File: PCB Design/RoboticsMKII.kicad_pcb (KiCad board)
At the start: 4 copper layers, 93 parts, among them CON1 USB, CON2 BARREL_JACK, P1 Power Sel, P10 CONN_02X12, P11 DAC, P12 Reed, P13 SPI, P14 ICSP, P15 Gnd, P16 UART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

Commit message: Some changes?
Signed-off-by: Kolijn Wolfaardt <kolijn.wolfaardt@gmail.com>
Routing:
- net (no net): track 5.21 -> 0.13 mm, vias 15 -> 16
- net /mcu/MOT2_D1: track 39.0 -> 40.8 mm
- net GND: track 589.0 -> 588.5 mm
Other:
- board text added: "v1.00"
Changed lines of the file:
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@@
     (area 108.284333 35.228 170.003334 143.996)
     (thickness 1.6)
-    (drawings 6)
-    (tracks 1643)
+    (drawings 7)
+    (tracks 1646)
     (zones 0)
     (modules 93)
@@
     (mod_text_size 0.7 0.7)
     (mod_text_width 0.1)
-    (pad_size 4 4)
-    (pad_drill 3)
+    (pad_size 3.50012 3.50012)
+    (pad_drill 2.99974)
     (pad_to_mask_clearance 0)
     (aux_axis_origin 0 0)
@@
     (visible_elements FFFFF7FF)
     (pcbplotparams
-      (layerselection 0x000f0_80000007)
-      (usegerberextensions false)
+      (layerselection 0x001f0_80000007)
+      (usegerberextensions true)
       (excludeedgelayer true)
       (linewidth 0.100000)
-      (plotframeref true)
+      (plotframeref false)
       (viasonmask false)
       (mode 1)
@@
     (fp_line (start 7.00024 4.50088) (end 7.00024 -4.50088) (layer F.SilkS) (width 0.15))
     (fp_line (start 7.00024 -4.50088) (end -7.50062 -4.50088) (layer F.SilkS) (width 0.15))
-    (pad 1 thru_hole rect (at 6.20014 0 270) (size 3.50012 3.50012) (drill oval 1.00076 2.99974) (layers *.Cu *.Mask F.SilkS)
+    (pad 1 thru_hole rect (at 6.20014 0 270) (size 3.50012 3.50012) (drill oval 2.99974) (layers *.Cu *.Mask F.SilkS)
       (net 21 "Net-(CON2-Pad1)"))
-    (pad 2 thru_hole rect (at 0.20066 0 270) (size 3.50012 3.50012) (drill oval 1.00076 2.99974) (layers *.Cu *.Mask F.SilkS)
+    (pad 2 thru_hole rect (at 0.20066 0 270) (size 3.50012 3.50012) (drill oval 2.99974) (layers *.Cu *.Mask F.SilkS)
       (net 2 GND))
-    (pad 3 thru_hole rect (at 3.2004 4.699 270) (size 3.50012 3.50012) (drill oval 2.99974 1.00076) (layers *.Cu *.Mask F.SilkS)
+    (pad 3 thru_hole rect (at 3.2004 4.699 270) (size 3.50012 3.50012) (drill oval 2.99974) (layers *.Cu *.Mask F.SilkS)
       (net 22 "Net-(CON2-Pad3)"))
   )
@@
     )
   )
+  (gr_text v1.00 (at 145.796 90.932) (layer F.SilkS)
+    (effects (font (size 0.7 0.7) (thickness 0.12)))
+  )
   (gr_text https://github.com/KolijnWolfaardt/RoBoC (at 138.43 117.856) (layer F.SilkS)
     (effects (font (size 0.7 0.7) (thickness 0.12)))
@@
   (via (at 115.316 97.536) (size 0.6) (layers F.Cu B.Cu) (net 0))
   (via (at 152.908 64.516) (size 0.6) (layers F.Cu B.Cu) (net 0))
-  (via (at 116.84 82.55) (size 0.6) (layers F.Cu B.Cu) (net 0))
-  (segment (start 121.92 82.55) (end 116.84 82.55) (width 0.25) (layer In2.Cu) (net 0))
   (via (at 117.348 50.419) (size 0.6) (layers F.Cu B.Cu) (net 0))
   (via (at 119.888 48.133) (size 0.6) (layers F.Cu B.Cu) (net 0))
@@
   (via (at 139.573 52.832) (size 0.6) (layers F.Cu B.Cu) (net 0))
   (via (at 151.384 61.722) (size 0.6) (layers F.Cu B.Cu) (net 0))
+  (via (at 116.586 82.55) (size 0.6) (layers F.Cu B.Cu) (net 0))
+  (via (at 126.746 82.423) (size 0.6) (layers F.Cu B.Cu) (net 0))
   (via (at 141.478 49.53) (size 0.6) (layers F.Cu B.Cu) (net 1))
   (segment (start 143.48 48.29) (end 142.24 49.53) (width 0.4) (layer B.Cu) (net 1))
@@
   (segment (start 153.825 51.661) (end 154.051 51.435) (width 0.25) (layer B.Cu) (net 2))
   (segment (start 146.304 96.901) (end 143.129 96.901) (width 0.25) (layer B.Cu) (net 2))
-  (segment (start 129.45 65.095) (end 132.263 65.095) (width 0.25) (layer F.Cu) (net 2))
-  (segment (start 132.842 64.516) (end 132.842 62.23) (width 0.25) (layer F.Cu) (net 2))
-  (segment (start 132.263 65.095) (end 132.842 64.516) (width 0.25) (layer F.Cu) (net 2))
   (segment (start 118.618 130.556) (end 114.608 130.556) (width 0.25) (layer F.Cu) (net 2))
   (segment (start 114.608 130.556) (end 114.572 130.52) (width 0.25) (layer F.Cu) (net 2))
@@
   (segment (start 146.812 48.768) (end 146.08 48.036) (width 0.25) (layer B.Cu) (net 2))
   (via (at 145.034 52.324) (size 0.6) (layers F.Cu B.Cu) (net 2))
-  (segment (start 136.398 60.706) (end 132.334 60.706) (width 0.25) (layer F.Cu) (net 2))
   (segment (start 133.985 62.635) (end 133.985 62.357) (width 0.25) (layer B.Cu) (net 2))
-  (segment (start 126.746 60.706) (end 132.334 60.706) (width 0.25) (layer F.Cu) (net 2))
-  (segment (start 126.746 60.706) (end 124.714 60.706) (width 0.25) (layer F.Cu) (net 2))
   (segment (start 124.714 60.706) (end 123.952 60.706) (width 0.25) (layer F.Cu) (net 2))
   (segment (start 123.952 60.706) (end 121.412 60.706) (width 0.25) (layer F.Cu) (net 2))
-  (segment (start 132.842 62.23) (end 132.842 61.214) (width 0.25) (layer F.Cu) (net 2))
-  (segment (start 132.334 60.706) (end 132.842 61.214) (width 0.25) (layer F.Cu) (net 2))
-  (segment (start 135.128 63.795) (end 134.407 63.795) (width 0.25) (layer F.Cu) (net 2))
-  (segment (start 134.407 63.795) (end 132.842 62.23) (width 0.25) (layer F.Cu) (net 2))
   (segment (start 136.25 63.795) (end 135.128 63.795) (width 0.25) (layer F.Cu) (net 2))
   (segment (start 135.128 63.795) (end 135.169 63.795) (width 0.25) (layer F.Cu) (net 2))
@@
   (segment (start 119.888 113.03) (end 119.888 115.316) (width 0.25) (layer F.Cu) (net 2))
   (segment (start 119.888 115.316) (end 119.888 117.348) (width 0.25) (layer F.Cu) (net 2))
+  (segment (start 135.89 60.706) (end 135.509 60.325) (width 0.25) (layer F.Cu) (net 2))
+  (segment (start 133.731 60.325) (end 125.095 60.325) (width 0.25) (layer F.Cu) (net 2))
+  (segment (start 135.509 60.325) (end 133.731 60.325) (width 0.25) (layer F.Cu) (net 2))
+  (segment (start 125.095 60.325) (end 124.714 60.706) (width 0.25) (layer F.Cu) (net 2))
+  (segment (start 136.398 60.706) (end 135.89 60.706) (width 0.25) (layer F.Cu) (net 2))
+  (segment (start 133.731 63.5) (end 133.731 60.325) (width 0.25) (layer F.Cu) (net 2))
+  (segment (start 129.45 65.095) (end 132.263 65.095) (width 0.25) (layer F.Cu) (net 2))
+  (segment (start 132.263 65.095) (end 132.842 64.516) (width 0.25) (layer F.Cu) (net 2))
+  (segment (start 133.731 63.627) (end 133.731 63.5) (width 0.25) (layer F.Cu) (net 2))
+  (segment (start 132.842 64.516) (end 133.731 63.627) (width 0.25) (layer F.Cu) (net 2))
+  (segment (start 134.026 63.795) (end 133.731 63.5) (width 0.25) (layer F.Cu) (net 2))
+  (segment (start 135.128 63.795) (end 134.407 63.795) (width 0.25) (layer F.Cu) (net 2))
+  (segment (start 134.407 63.795) (end 134.026 63.795) (width 0.25) (layer F.Cu) (net 2))
   (segment (start 142.216 103.378) (end 142.216 101.576) (width 0.25) (layer B.Cu) (net 3))
   (segment (start 142.216 101.576) (end 140.97 100.33) (width 0.25) (layer B.Cu) (net 3))
@@
   (segment (start 140.97 67.818) (end 139.547 66.395) (width 0.25) (layer F.Cu) (net 85))
   (segment (start 137.25 66.395) (end 139.547 66.395) (width 0.25) (layer F.Cu) (net 85))
-  (via (at 140.97 71.247) (size 0.6) (layers F.Cu B.Cu) (net 85))
-  (segment (start 140.97 71.247) (end 140.97 70.104) (width 0.25) (layer F.Cu) (net 85))
+  (via (at 140.97 69.215) (size 0.6) (layers F.Cu B.Cu) (net 85))
+  (segment (start 140.97 69.215) (end 140.97 70.104) (width 0.25) (layer F.Cu) (net 85))
   (segment (start 144.526 92.71) (end 144.018 92.202) (width 0.25) (layer B.Cu) (net 85))
   (via (at 144.526 92.71) (size 0.6) (layers F.Cu B.Cu) (net 85))
@@
   (segment (start 144.018 87.884) (end 140.97 84.836) (width 0.25) (layer B.Cu) (net 85))
   (segment (start 144.018 92.202) (end 144.018 87.884) (width 0.25) (layer B.Cu) (net 85))
-  (segment (start 140.97 75.438) (end 140.97 71.247) (width 0.25) (layer B.Cu) (net 85))
+  (segment (start 140.97 75.438) (end 140.97 69.215) (width 0.25) (layer B.Cu) (net 85))
   (segment (start 140.97 70.104) (end 140.97 67.818) (width 0.25) (layer F.Cu) (net 85))
   (segment (start 145.936998 97.58) (end 146.304 97.212998) (width 0.25) (layer F.Cu) (net 85))

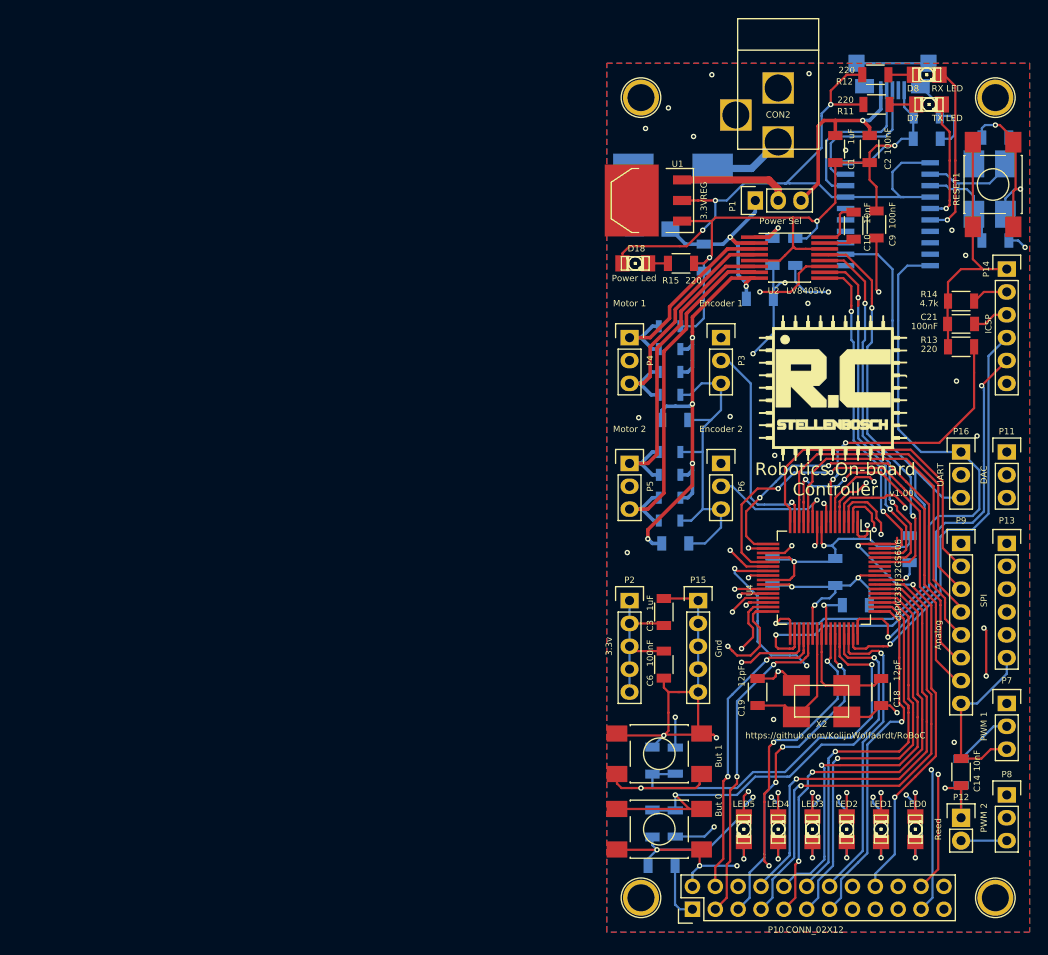
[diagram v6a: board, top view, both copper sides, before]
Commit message: Started 2 layer layout
Signed-off-by: Kolijn Wolfaardt <kolijn.wolfaardt@gmail.com>
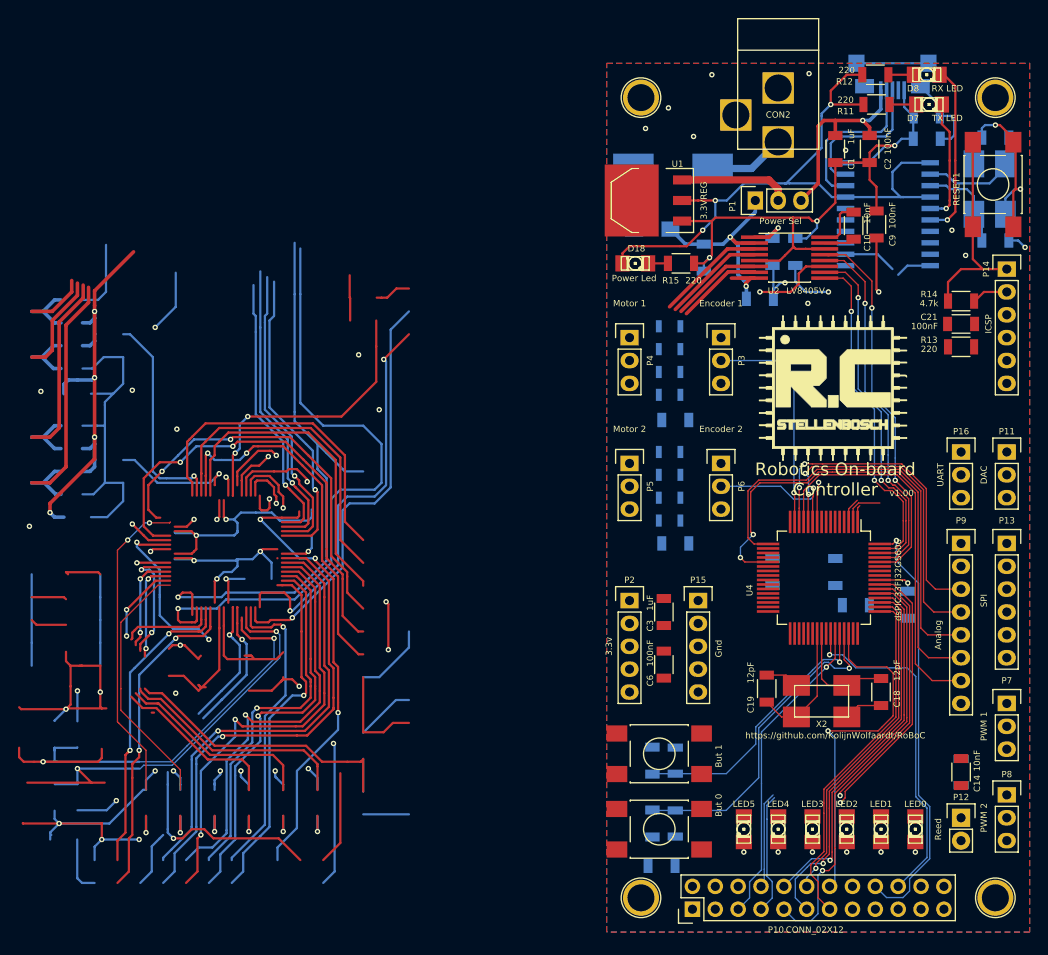
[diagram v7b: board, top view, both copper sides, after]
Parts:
- moved C20 6.18 mm to (146.5, 103.3), turned to 90 degrees
- moved C19 1.09 mm to (130.8, 112.6)
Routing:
- net (no net): track 0.13 -> 3276.9 mm, vias 16 -> 118
- net GND: track 588.5 -> 116.0 mm, vias 25 -> 7
- net V3.3: track 479.8 -> 102.4 mm, vias 13 -> 7
- net /usb/MCU_RX: track 73.9 -> 3.98 mm, vias 1 -> 0
- net /usb/MCU_TX: track 71.4 -> 5.89 mm, vias 1 -> 0
- net /gpio/~WRST: track 58.0 -> 0.00 mm, vias 3 -> 0
- net /gpio/~RRST: track 53.2 -> 0.00 mm, vias 2 -> 0
- net /gpio/Href: track 53.2 -> 0.00 mm, vias 1 -> 0
- net /gpio/~WR: track 53.2 -> 0.00 mm, vias 1 -> 0
- net /motors/V_Bat: track 79.7 -> 27.6 mm, vias 6 -> 2
- net /gpio/Reed: track 48.9 -> 0.00 mm, vias 2 -> 0
- net /mcu/PGD: track 46.9 -> 0.00 mm, vias 1 -> 0
- net /mcu/PGC: track 44.9 -> 0.00 mm, vias 2 -> 0
- net /motors/PWM2: track 47.4 -> 2.81 mm, vias 3 -> 0
- net /gpio/DACOUT: track 42.9 -> 0.00 mm, vias 1 -> 0
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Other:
- net class Default: clearance 0.2 -> 0.15; trace_width 0.25 -> 0.15
- rule trace_clearance: 0.2 -> 0.15
- rule trace_min: 0.2 -> 0.15

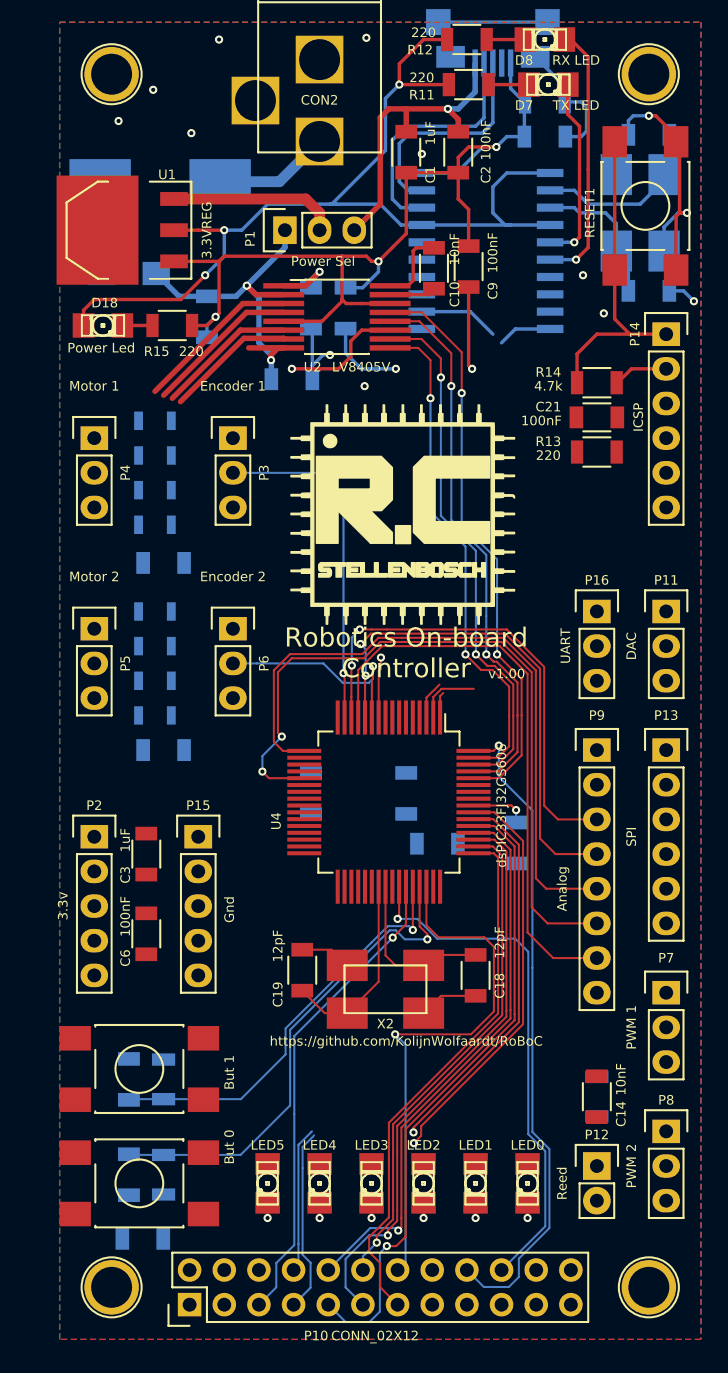
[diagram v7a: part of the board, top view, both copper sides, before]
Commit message: Many buslines done, camera bus almost there, LED bus almost done, analog bus almost. SPI and pwm needs attention
Signed-off-by: Kolijn Wolfaardt <kolijn.wolfaardt@gmail.com>
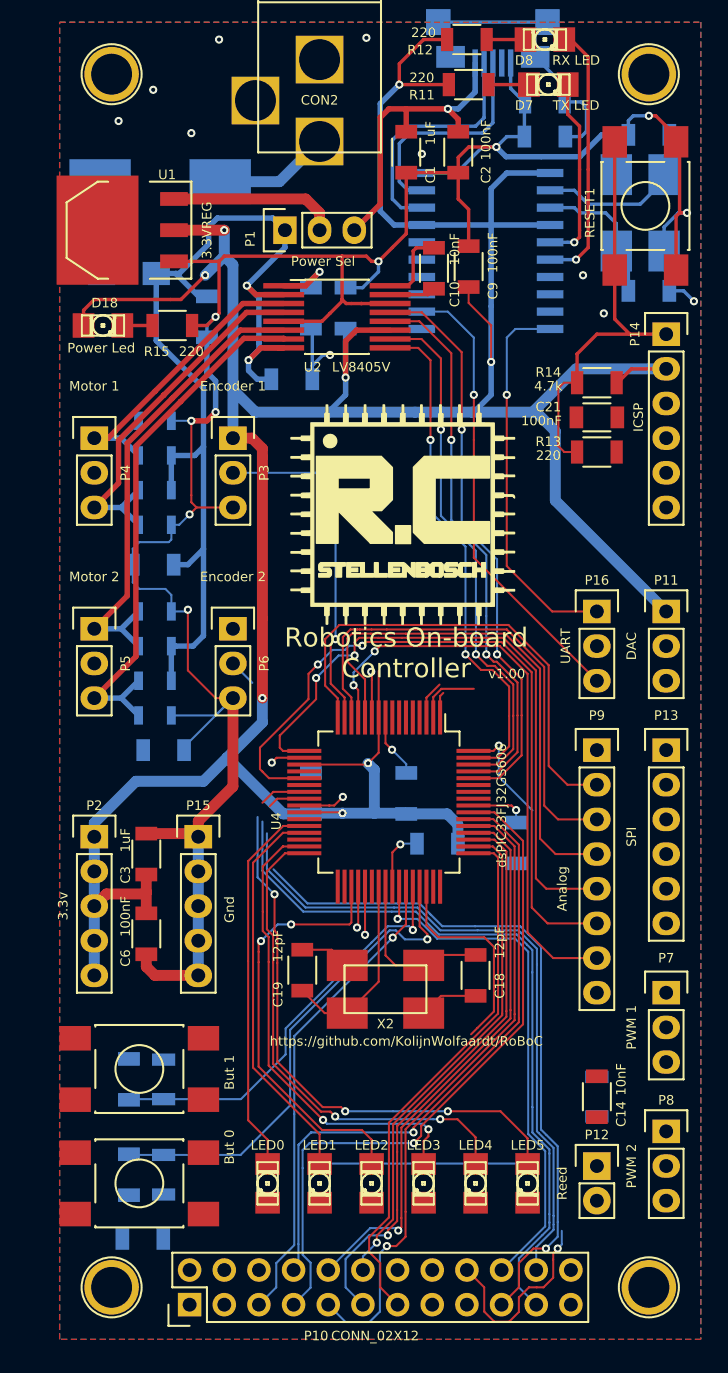
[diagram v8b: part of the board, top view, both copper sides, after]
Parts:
- moved D1 19.0 mm to (147.3, 128.3)
- moved D6 19.0 mm to (128.3, 128.3)
- moved R1 19.0 mm to (147.3, 128.3)
- moved R8 19.0 mm to (128.3, 128.3)
- moved D2 11.4 mm to (143.5, 128.3)
- moved D5 11.4 mm to (132.1, 128.3)
- moved R3 11.4 mm to (143.5, 128.3)
- moved R6 11.4 mm to (132.1, 128.3)
- moved D3 3.81 mm to (139.7, 128.3)
- moved D4 3.81 mm to (135.9, 128.3)
- moved R4 3.81 mm to (139.7, 128.3)
- moved R5 3.81 mm to (135.9, 128.3)
- moved C25 0.77 mm to (119.9, 82.9), turned to 180 degrees
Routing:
- net V3.3: track 102.4 -> 258.2 mm, vias 7 -> 8
- net GND: track 116.0 -> 237.0 mm, vias 7 -> 14
- net /gpio/~WRST: track 0.00 -> 57.2 mm
- net /gpio/~RRST: track 0.00 -> 52.2 mm
- net /gpio/~WR: track 0.00 -> 50.9 mm, vias 0 -> 1
- net /motors/V_Bat: track 27.6 -> 76.6 mm
- net /gpio/LED5: track 0.00 -> 44.1 mm, vias 0 -> 4
- net /gpio/LED4: track 0.00 -> 36.6 mm, vias 0 -> 2
- net /gpio/AN0: track 0.00 -> 35.6 mm
- net /gpio/LED3: track 0.00 -> 34.8 mm, vias 0 -> 2
- net /gpio/LED2: track 0.00 -> 31.4 mm, vias 0 -> 2
- net /motors/MOT2_2: track 9.54 -> 39.5 mm
- net /gpio/LED1: track 0.00 -> 28.8 mm
- net /gpio/LED0: track 0.00 -> 28.0 mm
- net /usb/MCU_TX: track 5.89 -> 33.5 mm, vias 0 -> 1
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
